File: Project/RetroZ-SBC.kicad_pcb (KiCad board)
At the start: 4 copper layers, 99.7 x 87.6 mm, 40 parts, among them J1 Master Bus, J2 POWER, SW1 RESET, SW2 Off/On, U1 74HCT04, U10 Z84C3008PEG, U11 74LS138, U12 L7805CV-DG, U2 max699cpa, U3 74LS32, U4 74LS08, U5 Z80CPU, U6 74HC273, U7 74LS08-And2, U8 AT28C64B-15PU, U9 AS6C4008-55PCN, Y1 7.3728Mhz

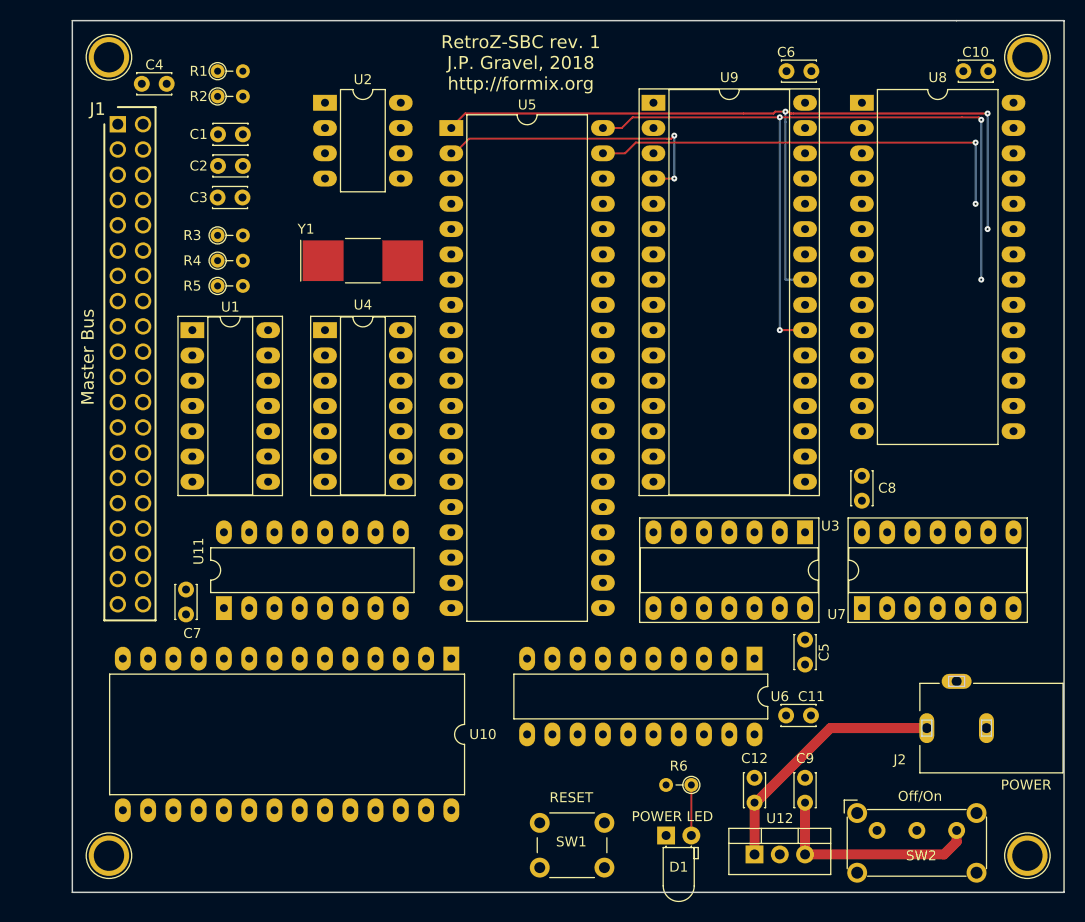
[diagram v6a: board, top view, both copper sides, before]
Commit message: removed ctc
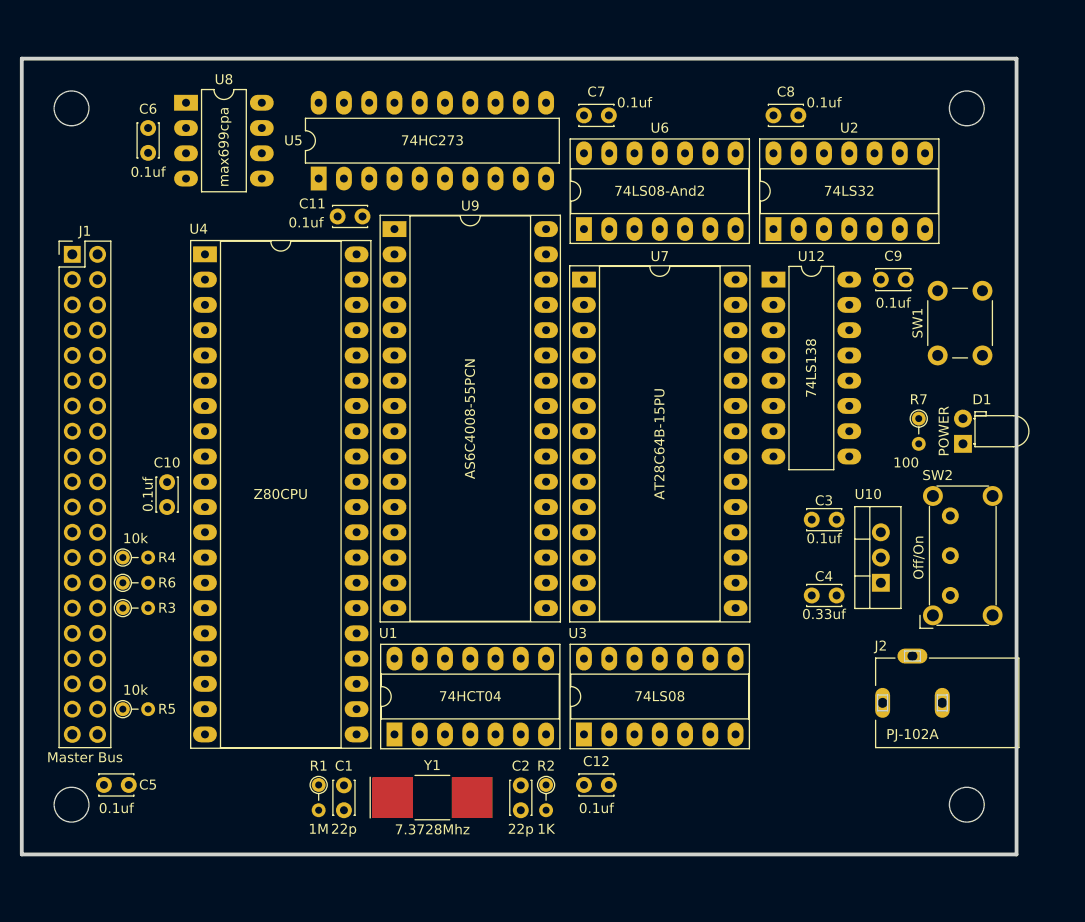
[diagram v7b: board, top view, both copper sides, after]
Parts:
- removed the REF** at (109.1, 137.3)
- removed the REF** at (109.1, 57.0)
- removed the REF** at (201.4, 57.0)
- removed the REF** at (201.4, 137.3)
- removed U11: 74LS138, Housings_DIP:DIP-16_W7.62mm_LongPads
- added R7: 100, Resistors_THT:R_Axial_DIN0204_L3.6mm_D1.6mm_P2.54mm_Vertical, F.Cu at (190.5, 93.3)
- added REF**: EuroBoard_halb_Type-I_100mmX80mm_holes, EuroBoard_Outline:EuroBoard_halb_Type-I_100mmX80mm_holes, F.Cu at (100.3, 137.2)
- C12: value 0.33uf -> 0.1uf
- C4: value 0.1uf -> 0.33uf
- D1: value POWER LED -> POWER
- J1: footprint SystemBus2:SHDR40W64P254_2X20_5130X500X865P -> Pin_Headers:Pin_Header_Straight_2x20_Pitch2.54mm
- J2: value POWER -> PJ-102A
- R6: value 100 -> 10k
- U10: value Z84C3008PEG -> L7805CV-DG; footprint Housings_DIP:DIP-28_W15.24mm_LongPads -> TO_SOT_Packages_THT:TO-220-3_Vertical
- U12: value L7805CV-DG -> 74LS138; footprint TO_SOT_Packages_THT:TO-220-3_Vertical -> Housings_DIP:DIP-16_W7.62mm_LongPads
- U2: value max699cpa -> 74LS32; footprint Housings_DIP:DIP-8_W7.62mm_LongPads -> Housings_DIP:DIP-14_W7.62mm_Socket_LongPads
- U3: value 74LS32 -> 74LS08
- U4: value 74LS08 -> Z80CPU; footprint Housings_DIP:DIP-14_W7.62mm_Socket_LongPads -> Housings_DIP:DIP-40_W15.24mm_Socket_LongPads
- U5: value Z80CPU -> 74HC273; footprint Housings_DIP:DIP-40_W15.24mm_LongPads -> Housings_DIP:DIP-20_W7.62mm_LongPads
- U6: value 74HC273 -> 74LS08-And2; footprint Housings_DIP:DIP-20_W7.62mm_LongPads -> Housings_DIP:DIP-14_W7.62mm_Socket_LongPads
- U7: value 74LS08-And2 -> AT28C64B-15PU; footprint Housings_DIP:DIP-14_W7.62mm_Socket_LongPads -> Housings_DIP:DIP-28_W15.24mm_Socket_LongPads
- U8: value AT28C64B-15PU -> max699cpa; footprint Housings_DIP:DIP-28_W15.24mm_LongPads -> Housings_DIP:DIP-8_W7.62mm_LongPads
- moved C10 93.5 mm to (114.9, 102.2), turned to 90 degrees
- moved C4 86.7 mm to (182.2, 111.1), turned to 180 degrees
- moved R2 76.7 mm to (153.0, 130.2), turned to 270 degrees
- moved R1 72.5 mm to (130.2, 130.2), turned to 270 degrees
- moved C5 72.0 mm to (108.6, 130.2), turned to 0 degrees
- moved C2 70.5 mm to (150.5, 132.7), turned to 90 degrees
- moved C3 70.2 mm to (182.2, 103.5), turned to 180 degrees
- moved C1 68.7 mm to (132.7, 132.7), turned to 90 degrees
- moved U8 67.9 mm to (116.8, 61.6)
- moved C11 67.4 mm to (132.1, 73.0)
- moved C6 66.9 mm to (113.0, 64.1), turned to 270 degrees
- moved C7 64.2 mm to (156.8, 62.9), turned to 0 degrees
- moved SW1 61.7 mm to (192.4, 87.0), turned to 90 degrees
- moved R6 60.7 mm to (110.5, 109.9), turned to 0 degrees
- moved U12 57.8 mm to (175.9, 79.4)
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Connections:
- C12 pad 1: Net-(C12-Pad1) -> VCC
- C3 pad 1: VCC -> Net-(C3-Pad1)
- C4 pad 1: VCC -> Net-(C4-Pad1)
- C9 pad 1: Net-(C9-Pad1) -> VCC
- J1 pad 1: VCC -> /A0
- J1 pad 10: IEO -> /A9
- J1 pad 11: ~IO0 -> /A10
- J1 pad 12: ~IO1 -> /A11
- J1 pad 13: ~IO2 -> /A12
- J1 pad 14: ~IO3 -> /A13
- J1 pad 15: ~IO4 -> /A14
- J1 pad 16: ~IO5 -> A15
- J1 pad 17: ~IO6 -> /D0
- J1 pad 18: ~IO7 -> /D1
- J1 pad 19: Net-(J1-Pad19) -> /D2
- J1 pad 2: ~M1 -> /A1
- J1 pad 20: Net-(J1-Pad20) -> /D3
- J1 pad 21: Net-(J1-Pad21) -> /D4
- J1 pad 22: Net-(J1-Pad22) -> /D5
- J1 pad 23: CLK0 -> /D6
- J1 pad 24: CLK1 -> /D7
- J1 pad 25: CLK2 -> ~INT
- J1 pad 26: /D0 -> CLK
- J1 pad 27: /D1 -> Net-(J1-Pad27)
- J1 pad 28: /D2 -> ~RESET
- J1 pad 29: /D3 -> ~BUSREQ
- J1 pad 3: ~IORQ -> /A2
- J1 pad 30: /D4 -> ~RD
- J1 pad 31: /D5 -> ~BUSACK
- J1 pad 32: /D6 -> ~WR
- J1 pad 33: /D7 -> ~M1
- J1 pad 34: A0 -> ~MREQ
- J1 pad 35: A1 -> Net-(J1-Pad35)
- J1 pad 36: A2 -> ~IORQ
- J1 pad 37: A3 -> Net-(J1-Pad37)
- J1 pad 38: A7 -> ~WAIT
- J1 pad 39: CLK -> VCC
- J1 pad 4: ~RD -> /A3
- J1 pad 5: ~WR -> /A4
- J1 pad 6: ~HALT -> /A5
- J1 pad 7: ~WAIT -> /A6
- J1 pad 8: ~INT -> /A7
- J1 pad 9: ~RESET -> /A8
- J2 pad 1: Net-(C12-Pad1) -> Net-(C4-Pad1)
- R3 pad 1: ~INT -> ~BUSREQ
- R4 pad 1: ~WAIT -> ~INT
- R5 pad 1: ~RESET -> ~WAIT
- R6 pad 1: Net-(D1-Pad2) -> ~RESET
- SW2 pad 3: Net-(C9-Pad1) -> Net-(C3-Pad1)
- U1 pad 5: ~IO0 -> Net-(U1-Pad5)
- U10 pad 1: /D4 -> Net-(C4-Pad1)
- U10 pad 2: /D5 -> GND
- U10 pad 3: /D6 -> Net-(C3-Pad1)
- U12 pad 1: Net-(C12-Pad1) -> /A4
- U12 pad 2: GND -> /A5
- U12 pad 3: Net-(C9-Pad1) -> /A6
- U2 pad 1: VCC -> ~MREQ
- U2 pad 2: VCC -> ~RD
- U2 pad 3: GND -> ~MRD
- U2 pad 4: GND -> ~WR
- U2 pad 5: Net-(U2-Pad5) -> ~MREQ
- U2 pad 6: Net-(U2-Pad6) -> ~MWR
- U2 pad 7: ~RESET -> GND
- U2 pad 8: GND -> Net-(U2-Pad12)
- U3 pad 1: Net-(U3-Pad1) -> Net-(U1-Pad6)
- U3 pad 10: /A14 -> Net-(U1-Pad8)
- U3 pad 11: Net-(U1-Pad9) -> (no net)
- U3 pad 12: Net-(U3-Pad12) -> (no net)
- U3 pad 13: A15 -> (no net)
- U3 pad 2: ~RD -> CLK
- U3 pad 3: ~MRD -> Net-(U3-Pad3)
- U3 pad 4: ~WR -> RAMONLY
- U3 pad 5: Net-(U3-Pad1) -> A15
- U3 pad 6: ~MWR -> Net-(U3-Pad6)
- U3 pad 8: Net-(U3-Pad12) -> ~RAM_SEL
- U3 pad 9: /A13 -> Net-(U1-Pad10)
- U4 pad 1: Net-(U1-Pad6) -> /A11
- U4 pad 10: Net-(U1-Pad8) -> /D6
- U4 pad 11: (no net) -> VCC
- U4 pad 12: (no net) -> /D2
- U4 pad 13: (no net) -> /D7
- U4 pad 14: VCC -> /D0
- U4 pad 2: CLK -> /A12
- U4 pad 3: Net-(U4-Pad3) -> /A13
- U4 pad 4: RAMONLY -> /A14
- U4 pad 6: Net-(U4-Pad6) -> CLK
- U4 pad 7: GND -> /D4
- U4 pad 8: ~RAM_SEL -> /D3
- U4 pad 9: Net-(U1-Pad10) -> /D5
- U5 pad 1: /A11 -> ~RESET
- U5 pad 10: /D6 -> GND
- U5 pad 11: VCC -> Net-(U3-Pad3)
- U5 pad 12: /D2 -> RAMONLY
- U5 pad 13: /D7 -> /D4
- U5 pad 14: /D0 -> GND
- U5 pad 15: /D1 -> Net-(U5-Pad15)
- U5 pad 16: ~INT -> Net-(U5-Pad16)
- U5 pad 17: VCC -> GND
- U5 pad 18: ~HALT -> GND
- U5 pad 19: Net-(U3-Pad1) -> Net-(U5-Pad19)
- U5 pad 2: /A12 -> Net-(U5-Pad2)
- U5 pad 20: ~IORQ -> VCC
- U5 pad 3: /A13 -> /D0
- U5 pad 4: /A14 -> /D1
- U5 pad 5: A15 -> Net-(U5-Pad5)
- U5 pad 6: CLK -> Net-(U5-Pad6)
- U5 pad 7: /D4 -> /D2
- U5 pad 9: /D5 -> Net-(U5-Pad9)
- U6 pad 1: ~RESET -> Net-(U5-Pad2)
- U6 pad 10: GND -> Net-(U3-Pad6)
- U6 pad 11: Net-(U4-Pad3) -> RAM_A18
- U6 pad 12: RAMONLY -> Net-(U5-Pad9)
- U6 pad 13: /D4 -> Net-(U3-Pad6)
- U6 pad 14: GND -> VCC
- U6 pad 2: Net-(U6-Pad2) -> Net-(U3-Pad6)
- U6 pad 3: /D0 -> RAM_A15
- U6 pad 4: /D1 -> Net-(U5-Pad5)
- U6 pad 5: Net-(U6-Pad5) -> Net-(U3-Pad6)
- U6 pad 6: Net-(U6-Pad6) -> RAM_A16
- U6 pad 7: /D2 -> GND
- U6 pad 8: /D3 -> RAM_A17
- U6 pad 9: Net-(U6-Pad9) -> Net-(U5-Pad6)
- U7 pad 1: Net-(U6-Pad2) -> Net-(U7-Pad1)
- U7 pad 10: Net-(U4-Pad6) -> /A0
- U7 pad 11: RAM_A18 -> /D0
- U7 pad 12: Net-(U6-Pad9) -> /D1
- U7 pad 13: Net-(U4-Pad6) -> /D2
- U7 pad 14: VCC -> GND
- U7 pad 2: Net-(U4-Pad6) -> /A12
- U7 pad 3: RAM_A15 -> /A7
- U7 pad 4: Net-(U6-Pad5) -> /A6
- U7 pad 5: Net-(U4-Pad6) -> /A5
- U7 pad 6: RAM_A16 -> /A4
- U7 pad 7: GND -> /A3
- U7 pad 8: RAM_A17 -> /A2
- U7 pad 9: Net-(U6-Pad6) -> /A1
- U8 pad 1: Net-(U8-Pad1) -> VCC
- U8 pad 2: /A12 -> VCC
- U8 pad 3: A7 -> GND
- U8 pad 4: /A6 -> GND
- U8 pad 5: /A5 -> Net-(U8-Pad5)
- U8 pad 6: /A4 -> Net-(U8-Pad6)
- U8 pad 7: A3 -> ~RESET
- U8 pad 8: A2 -> GND
- U9 pad 10: A2 -> /A2
- U9 pad 11: A1 -> /A1
- U9 pad 12: A0 -> /A0
- U9 pad 5: A7 -> /A7
- U9 pad 9: A3 -> /A3
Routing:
- net /A11: track 85.2 -> 0.00 mm, vias 3 -> 0
- net /A10: track 78.6 -> 0.00 mm, vias 4 -> 0
- net /A9: track 44.1 -> 0.00 mm, vias 2 -> 0
- net /A12: track 29.6 -> 0.00 mm, vias 2 -> 0
- net Net-(C12-Pad1): track 25.6 -> 0.00 mm
- net Net-(C9-Pad1): track 22.1 -> 0.00 mm
- net Net-(D1-Pad2): track 5.08 -> 0.00 mm
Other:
- board size 99.7 x 87.6 mm -> 100 x 80 mm
- board text removed: "RetroZ-SBC rev. 1 J.P. Gravel, 2018 http://formix.org"
